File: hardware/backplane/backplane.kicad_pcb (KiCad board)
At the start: 4 copper layers, 192 x 31.5 mm, 84 parts, among them J1 Bus_PCI_Express_x1, J2 PWR, J3 Bus_PCI_Express_x1, J4 Bus_PCI_Express_x1, J5 Bus_PCI_Express_x1, J6 Bus_PCI_Express_x1, J7 Bus_PCI_Express_x1, J8 Bus_PCI_Express_x1, M1 FAN1, Q1 IRFS7530TRL7PP, Q2 AO3400A, U1 AP64352SP-13, U2 TCA9548APWR, U3 TCA9539PWR, U4 LM74700

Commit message: fix(backplane): switch TVS diode to bidirectional
feat(backplane): swap fan FET for higher voltage spec
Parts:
- D1: value SMCJ33A -> SMCJ33CA
- Q2: value AO3400A -> IRLML0060TRPbF
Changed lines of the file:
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@@
 			)
 		)
-		(property "Value" "AO3400A"
+		(property "Value" "IRLML0060TRPbF"
 			(at 0 2.4 0)
 			(layer "F.Fab")
@@
 			)
 		)
-		(property "Datasheet" "http://www.aosmd.com/pdfs/datasheet/AO3400A.pdf"
+		(property "Datasheet" "https://www.infineon.com/assets/row/public/documents/24/49/infineon-irlml0060-datasheet-en.pdf"
 			(at 0 0 0)
 			(layer "F.Fab")
@@
 			)
 		)
-		(property "Description" "30V Vds, 5.7A Id, N-Channel MOSFET, SOT-23"
+		(property "Description" "60V Vds, 2.7A Id, N-Channel MOSFET, SOT-23"
 			(at 0 0 0)
 			(layer "F.Fab")
@@
 			)
 		)
-		(property "LCSC" "C20917"
+		(property "LCSC" "C67274"
 			(at 0 0 180)
 			(unlocked yes)
@@
 			)
 		)
-		(property "Value" "SMCJ33A"
+		(property "Value" "SMCJ33CA"
 			(at 0 4.2 0)
 			(layer "F.Fab")
@@
 			)
 		)
-		(property "LCSC" "C42371548"
+		(property "LCSC" "C310048"
 			(at 0 0 0)
 			(unlocked yes)

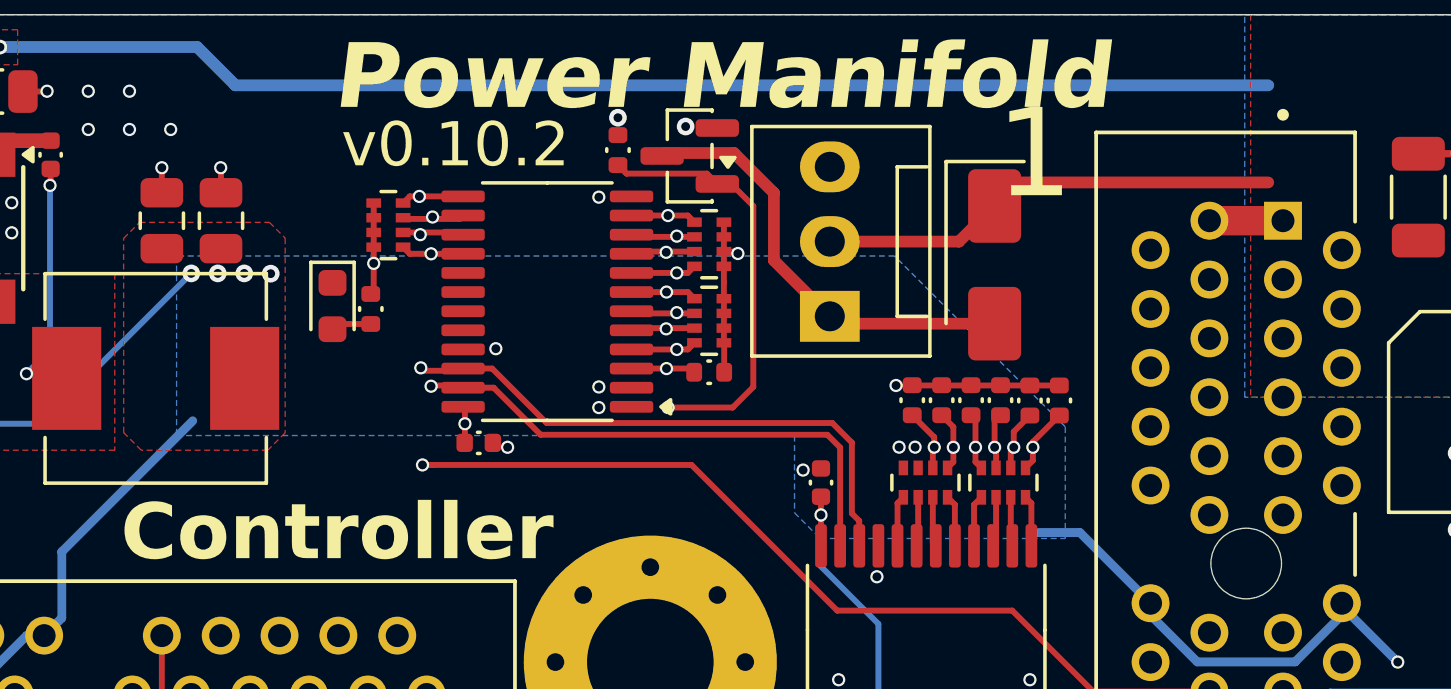
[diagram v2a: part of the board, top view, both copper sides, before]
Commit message: fix(backplane): switch fan from VIN to 5V supply
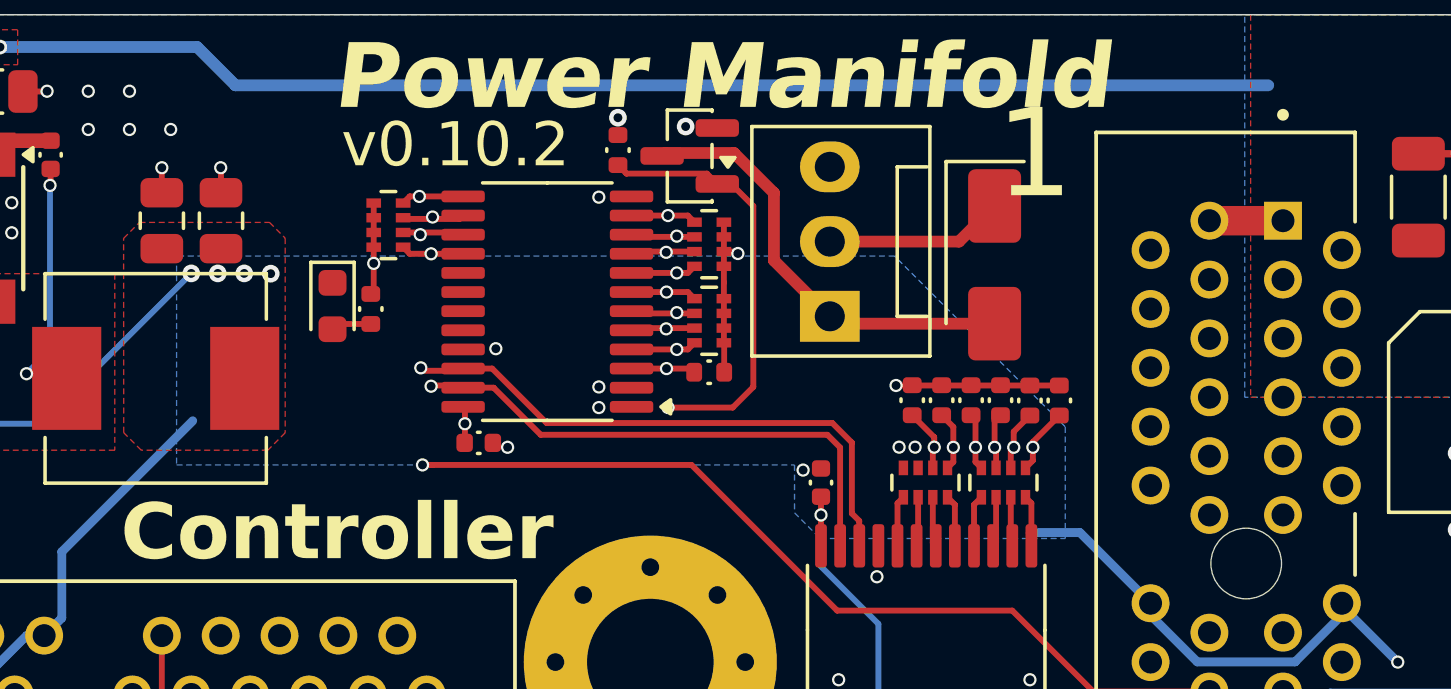
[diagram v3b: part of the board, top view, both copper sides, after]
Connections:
- D3 pad 1: VIN -> +5V
- M1 pad 2: VIN -> +5V
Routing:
- net VIN: track 115.1 -> 99.4 mm
- net +5V: track 250.2 -> 256.3 mm
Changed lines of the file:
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@@
 			(layers "*.Cu" "*.Mask")
 			(remove_unused_layers no)
-			(net "VIN")
+			(net "+5V")
 			(pinfunction "+_2")
 			(pintype "passive")
@@
 			(layers "F.Cu" "F.Mask" "F.Paste")
 			(roundrect_rratio 0.1388888889)
-			(net "VIN")
+			(net "+5V")
 			(pinfunction "K_1")
 			(pintype "passive")
@@
 	)
 	(segment
+		(start 71.1 57.71)
+		(end 75.49 57.71)
+		(width 0.4)
+		(layer "F.Cu")
+		(net "+5V")
+	)
+	(segment
 		(start 182.25 78.7)
 		(end 181.77 78.7)
@@
 		(net "+5V")
 	)
+	(segment
+		(start 75.49 57.71)
+		(end 76.7 56.5)
+		(width 0.4)
+		(layer "F.Cu")
+		(net "+5V")
+	)
 	(via
 		(at 90.4 72)
@@
 	)
 	(segment
-		(start 71.1 57.71)
-		(end 75.49 57.71)
-		(width 0.4)
-		(layer "F.Cu")
-		(net "VIN")
-	)
-	(segment
 		(start 194.925 75.725)
 		(end 204.175 75.725)
@@
 	)
 	(segment
-		(start 76.7 56.5)
-		(end 77.5 55.7)
-		(width 0.4)
-		(layer "F.Cu")
-		(net "VIN")
-	)
-	(segment
 		(start 205.6 74.3)
 		(end 205.6 74)
@@
 		(net "VIN")
 	)
-	(segment
-		(start 77.5 55.7)
-		(end 86 55.7)
-		(width 0.4)
-		(layer "F.Cu")
-		(net "VIN")
-	)
-	(segment
-		(start 75.49 57.71)
-		(end 76.7 56.5)
-		(width 0.4)
-		(layer "F.Cu")
-		(net "VIN")
-	)
 	(via
 		(at 188.3 60.1)
@@
 		(polygon
 			(pts
-				(xy 48.9 64.3) (xy 69.9 64.3) (xy 69.9 66.925) (xy 70.775 67.8) (xy 79.1 67.8) (xy 79.1 64) (xy 73.3 58.2)
+				(xy 48.9 65.3) (xy 69.9 65.3) (xy 69.9 66.925) (xy 70.775 67.8) (xy 79.1 67.8) (xy 79.1 64) (xy 73.3 58.2)
 				(xy 48.9 58.2)
 			)
